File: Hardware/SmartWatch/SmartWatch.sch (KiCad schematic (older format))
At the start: 78 parts, among them IC1 6PAIC3109TWRHMRQ1, IC2 SPG08P4HM4H-1, IC3 MC3630, J1 Charging Port, J2 DA_PROG_CONN, J3 ARD_PROG_CONN, J4 Adafruit 4520, M1 c0720b001f, Q1 ECH8693R-TL-W, Q2 ECH8693R-TL-W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

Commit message: [Update] Changes to schematic and PCB test layout
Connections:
- net labels removed: LA
- wire segments 368 -> 371
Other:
- note added: "NOTE: After programming the chip, \nconnect the pads of JP1 with soldier.\n"
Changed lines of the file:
@@
 LX
 Text Label 4150 2950 0    50   ~ 0
-LA
+LY
 Wire Notes Line width 39 style solid rgb(0, 0, 0)
 	8850 500  8850 11200
@@
 L power:GND #PWR021
 U 1 1 6280EB46
-P 7000 10550
-F 0 "#PWR021" H 7000 10300 50  0001 C CNN
-F 1 "GND" H 7005 10377 50  0000 C CNN
-F 2 "" H 7000 10550 50  0001 C CNN
-F 3 "" H 7000 10550 50  0001 C CNN
-	1    7000 10550
+P 7000 10600
+F 0 "#PWR021" H 7000 10350 50  0001 C CNN
+F 1 "GND" H 7005 10427 50  0000 C CNN
+F 2 "" H 7000 10600 50  0001 C CNN
+F 3 "" H 7000 10600 50  0001 C CNN
+	1    7000 10600
 	1    0    0    -1
 $EndComp
@@
 L power:GND #PWR023
 U 1 1 6282AB30
-P 7650 10550
-F 0 "#PWR023" H 7650 10300 50  0001 C CNN
-F 1 "GND" H 7655 10377 50  0000 C CNN
-F 2 "" H 7650 10550 50  0001 C CNN
-F 3 "" H 7650 10550 50  0001 C CNN
-	1    7650 10550
+P 7650 10600
+F 0 "#PWR023" H 7650 10350 50  0001 C CNN
+F 1 "GND" H 7655 10427 50  0000 C CNN
+F 2 "" H 7650 10600 50  0001 C CNN
+F 3 "" H 7650 10600 50  0001 C CNN
+	1    7650 10600
 	1    0    0    -1
 $EndComp
@@
 L power:GND #PWR025
 U 1 1 628469D8
-P 8300 10550
-F 0 "#PWR025" H 8300 10300 50  0001 C CNN
-F 1 "GND" H 8305 10377 50  0000 C CNN
-F 2 "" H 8300 10550 50  0001 C CNN
-F 3 "" H 8300 10550 50  0001 C CNN
-	1    8300 10550
+P 8300 10600
+F 0 "#PWR025" H 8300 10350 50  0001 C CNN
+F 1 "GND" H 8305 10427 50  0000 C CNN
+F 2 "" H 8300 10600 50  0001 C CNN
+F 3 "" H 8300 10600 50  0001 C CNN
+	1    8300 10600
 	1    0    0    -1
 $EndComp
@@
 NoConn ~ 13750 3800
 $Comp
-L power:+3V3 #PWR?
+L power:+3V3 #PWR0121
 U 1 1 61E41A65
 P 9800 3250
-F 0 "#PWR?" H 9800 3100 50  0001 C CNN
+F 0 "#PWR0121" H 9800 3100 50  0001 C CNN
 F 1 "+3V3" V 9815 3378 50  0000 L CNN
 F 2 "" H 9800 3250 50  0001 C CNN
@@
 $EndComp
 $Comp
-L power:+3V3 #PWR?
+L power:+3V3 #PWR0146
 U 1 1 61E945E7
 P 9800 3750
-F 0 "#PWR?" H 9800 3600 50  0001 C CNN
+F 0 "#PWR0146" H 9800 3600 50  0001 C CNN
 F 1 "+3V3" V 9815 3878 50  0000 L CNN
 F 2 "" H 9800 3750 50  0001 C CNN
@@
 $EndComp
 $Comp
-L power:GND #PWR?
+L power:GND #PWR0147
 U 1 1 61EBD732
 P 9800 3650
-F 0 "#PWR?" H 9800 3400 50  0001 C CNN
+F 0 "#PWR0147" H 9800 3400 50  0001 C CNN
 F 1 "GND" V 9800 3450 50  0000 C CNN
 F 2 "" H 9800 3650 50  0001 C CNN
@@
 NoConn ~ 9800 2950
 $Comp
-L power:GNDREF #PWR?
+L power:GNDREF #PWR0148
 U 1 1 620BCE8F
 P 13150 4100
-F 0 "#PWR?" H 13150 3850 50  0001 C CNN
+F 0 "#PWR0148" H 13150 3850 50  0001 C CNN
 F 1 "GNDREF" H 13155 3927 50  0000 C CNN
 F 2 "" H 13150 4100 50  0001 C CNN
@@
 $EndComp
 $Comp
-L power:GNDREF #PWR?
+L power:GNDREF #PWR0149
 U 1 1 620E6DE9
 P 15300 3700
-F 0 "#PWR?" H 15300 3450 50  0001 C CNN
+F 0 "#PWR0149" H 15300 3450 50  0001 C CNN
 F 1 "GNDREF" H 15305 3527 50  0000 C CNN
 F 2 "" H 15300 3700 50  0001 C CNN
@@
 $EndComp
 $Comp
-L power:GNDREF #PWR?
+L power:GNDREF #PWR0150
 U 1 1 621114A5
 P 3750 5500
-F 0 "#PWR?" H 3750 5250 50  0001 C CNN
+F 0 "#PWR0150" H 3750 5250 50  0001 C CNN
 F 1 "GNDREF" H 3755 5327 50  0000 C CNN
 F 2 "" H 3750 5500 50  0001 C CNN
@@
 	1    0    0    -1
 $EndComp
+Text Notes 14350 1200 0    50   ~ 0
+NOTE: After programming the chip, \nconnect the pads of JP1 with soldier.\n
+Wire Wire Line
+	7000 10550 7000 10600
+Wire Wire Line
+	7650 10550 7650 10600
+Wire Wire Line
+	8300 10550 8300 10600
 $EndSCHEMATC

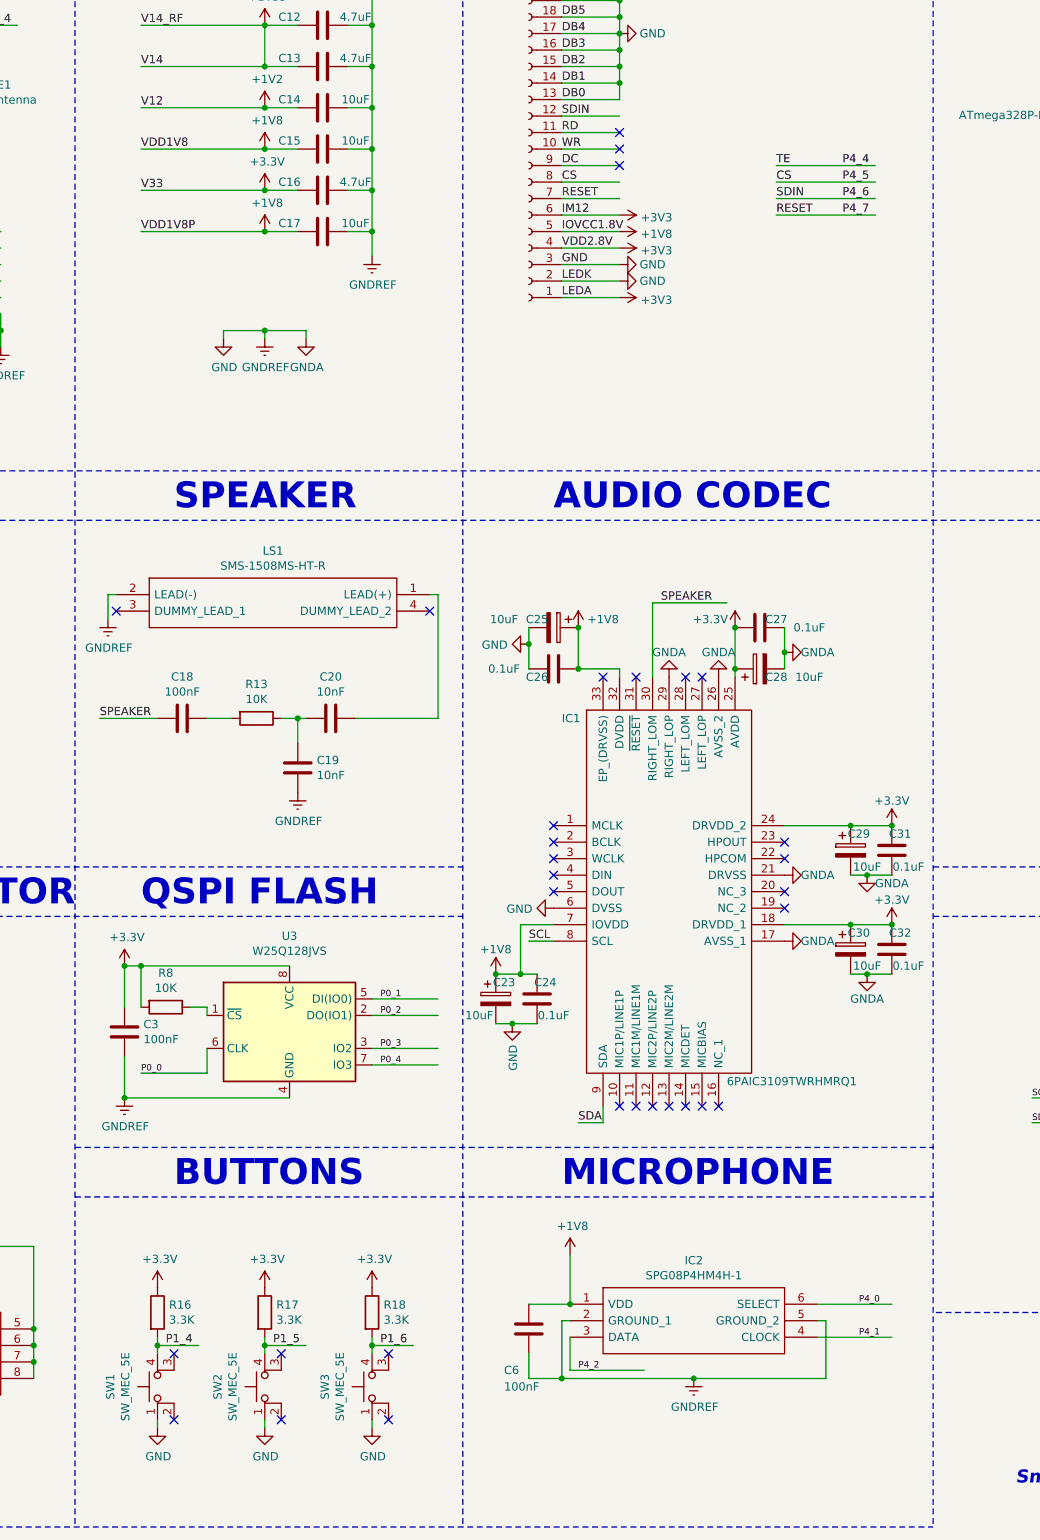
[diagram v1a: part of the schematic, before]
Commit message: [Update] Added communication with codec.
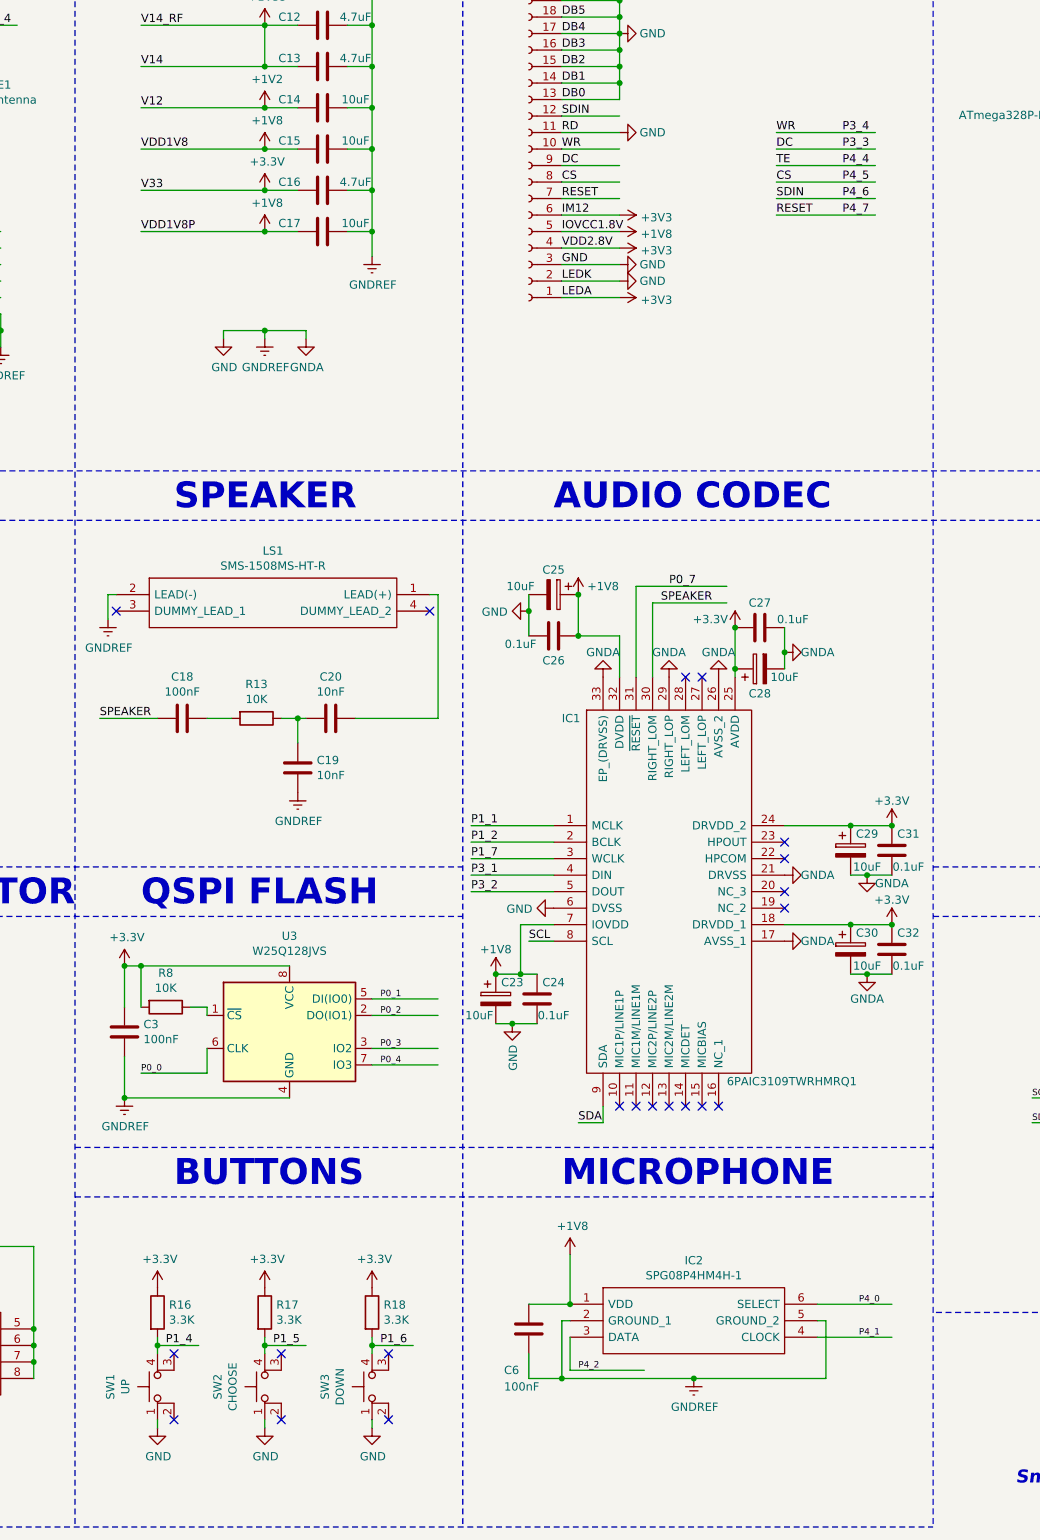
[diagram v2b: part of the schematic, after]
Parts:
- SW1: value SW_MEC_5E -> UP
- SW2: value SW_MEC_5E -> CHOOSE
- SW3: value SW_MEC_5E -> DOWN
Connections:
- wire segments 371 -> 380
- no-connect marks 58 -> 48
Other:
- moved on the sheet: C25, C26
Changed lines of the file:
@@
 U 1 1 630B89CE
 P 10650 5750
-F 0 "C27" V 10600 5850 50  0000 C CNN
-F 1 "0.1uF" V 10650 6050 50  0000 C CNN
+F 0 "C27" V 10500 5750 50  0000 C CNN
+F 1 "0.1uF" V 10600 5950 50  0000 C CNN
 F 2 "Capacitor_SMD:C_01005_0402Metric" H 10688 5600 50  0001 C CNN
 F 3 "~" H 10650 5750 50  0001 C CNN
@@
 U 1 1 6317A39A
 P 11450 7700
-F 0 "C32" H 11400 7600 50  0000 C CNN
+F 0 "C32" H 11350 7600 50  0000 C CNN
 F 1 "0.1uF" H 11350 7800 50  0000 C CNN
 F 2 "Capacitor_SMD:C_01005_0402Metric" H 11488 7550 50  0001 C CNN
@@
 U 1 1 630B9774
 P 10650 6000
-F 0 "C28" V 10600 5900 50  0000 C CNN
-F 1 "10uF" V 10600 5700 50  0000 C CNN
+F 0 "C28" V 10500 6000 50  0000 C CNN
+F 1 "10uF" V 10600 5850 50  0000 C CNN
 F 2 "Capacitor_SMD:C_01005_0402Metric" H 10688 5850 50  0001 C CNN
 F 3 "~" H 10650 6000 50  0001 C CNN
@@
 U 1 1 6317A3A0
 P 11200 7700
-F 0 "C30" H 11250 7800 50  0000 C CNN
+F 0 "C30" H 11300 7800 50  0000 C CNN
 F 1 "10uF" H 11300 7600 50  0000 C CNN
 F 2 "Capacitor_SMD:C_01005_0402Metric" H 11238 7550 50  0001 C CNN
@@
 U 1 1 632BFC59
 P 11450 7100
-F 0 "C31" H 11400 7000 50  0000 C CNN
+F 0 "C31" H 11350 7000 50  0000 C CNN
 F 1 "0.1uF" H 11350 7200 50  0000 C CNN
 F 2 "Capacitor_SMD:C_01005_0402Metric" H 11488 6950 50  0001 C CNN
@@
 U 1 1 632BFC60
 P 11200 7100
-F 0 "C29" H 11250 7200 50  0000 C CNN
+F 0 "C29" H 11300 7200 50  0000 C CNN
 F 1 "10uF" H 11300 7000 50  0000 C CNN
 F 2 "Capacitor_SMD:C_01005_0402Metric" H 11238 6950 50  0001 C CNN
@@
 L Device:C C26
 U 1 1 633C7CE9
-P 9400 6000
-F 0 "C26" V 9350 6100 50  0000 C CNN
-F 1 "0.1uF" V 9400 6300 50  0000 C CNN
-F 2 "Capacitor_SMD:C_01005_0402Metric" H 9438 5850 50  0001 C CNN
-F 3 "~" H 9400 6000 50  0001 C CNN
-	1    9400 6000
+P 9400 5800
+F 0 "C26" V 9250 5800 50  0000 C CNN
+F 1 "0.1uF" V 9350 6000 50  0000 C CNN
+F 2 "Capacitor_SMD:C_01005_0402Metric" H 9438 5650 50  0001 C CNN
+F 3 "~" H 9400 5800 50  0001 C CNN
+	1    9400 5800
 	0    -1   -1   0
 $EndComp
@@
 L Device:CP C25
 U 1 1 633C7CF8
-P 9400 5750
-F 0 "C25" V 9350 5650 50  0000 C CNN
-F 1 "10uF" V 9350 5450 50  0000 C CNN
-F 2 "Capacitor_SMD:C_01005_0402Metric" H 9438 5600 50  0001 C CNN
-F 3 "~" H 9400 5750 50  0001 C CNN
-	1    9400 5750
+P 9400 5550
+F 0 "C25" V 9250 5550 50  0000 C CNN
+F 1 "10uF" V 9350 5350 50  0000 C CNN
+F 2 "Capacitor_SMD:C_01005_0402Metric" H 9438 5400 50  0001 C CNN
+F 3 "~" H 9400 5550 50  0001 C CNN
+	1    9400 5550
 	0    1    1    0
 $EndComp
 Wire Wire Line
-	9550 6000 9550 5750
-Wire Wire Line
-	9250 6000 9250 5850
+	9550 5800 9550 5550
+Wire Wire Line
+	9250 5800 9250 5650
 $Comp
 L power:GND #PWR0133
 U 1 1 633EA102
-P 9250 5850
-F 0 "#PWR0133" H 9250 5600 50  0001 C CNN
-F 1 "GND" V 9255 5722 50  0000 R CNN
-F 2 "" H 9250 5850 50  0001 C CNN
-F 3 "" H 9250 5850 50  0001 C CNN
-	1    9250 5850
+P 9250 5650
+F 0 "#PWR0133" H 9250 5400 50  0001 C CNN
+F 1 "GND" V 9255 5522 50  0000 R CNN
+F 2 "" H 9250 5650 50  0001 C CNN
+F 3 "" H 9250 5650 50  0001 C CNN
+	1    9250 5650
 	0    1    1    0
 $EndComp
-Connection ~ 9250 5850
-Wire Wire Line
-	9250 5850 9250 5750
-Wire Wire Line
-	9800 6050 9800 6000
-Wire Wire Line
-	9800 6000 9550 6000
-Connection ~ 9550 6000
+Connection ~ 9250 5650
+Wire Wire Line
+	9250 5650 9250 5550
+Wire Wire Line
+	9800 5800 9550 5800
+Connection ~ 9550 5800
 $Comp
 L power:+1V8 #PWR0134
 U 1 1 6343113A
-P 9550 5750
-F 0 "#PWR0134" H 9550 5600 50  0001 C CNN
-F 1 "+1V8" H 9700 5800 50  0000 C CNN
-F 2 "" H 9550 5750 50  0001 C CNN
-F 3 "" H 9550 5750 50  0001 C CNN
-	1    9550 5750
-	1    0    0    -1
-$EndComp
-Connection ~ 9550 5750
+P 9550 5550
+F 0 "#PWR0134" H 9550 5400 50  0001 C CNN
+F 1 "+1V8" H 9700 5600 50  0000 C CNN
+F 2 "" H 9550 5550 50  0001 C CNN
+F 3 "" H 9550 5550 50  0001 C CNN
+	1    9550 5550
+	1    0    0    -1
+$EndComp
+Connection ~ 9550 5550
 $Comp
 L Device:C C24
 U 1 1 63433612
 P 9300 8000
-F 0 "C24" H 9250 7900 50  0000 C CNN
+F 0 "C24" H 9200 7900 50  0000 C CNN
 F 1 "0.1uF" H 9200 8100 50  0000 C CNN
 F 2 "Capacitor_SMD:C_01005_0402Metric" H 9338 7850 50  0001 C CNN
@@
 U 1 1 63433618
 P 9050 8000
-F 0 "C23" H 9100 8100 50  0000 C CNN
+F 0 "C23" H 9150 8100 50  0000 C CNN
 F 1 "10uF" H 8950 7900 50  0000 C CNN
 F 2 "Capacitor_SMD:C_01005_0402Metric" H 9088 7850 50  0001 C CNN
@@
 P 7100 10350
 F 0 "SW1" H 7100 10735 50  0000 C CNN
-F 1 "SW_MEC_5E" H 7100 10644 50  0000 C CNN
+F 1 "UP" H 7100 10644 50  0000 C CNN
 F 2 "Button_Switch_THT:SW_Tactile_SPST_Angled_PTS645Vx58-2LFS" H 7100 10650 50  0001 C CNN
 F 3 "http://www.apem.com/int/index.php?controller=attachment&id_attachment=1371" H 7100 10650 50  0001 C CNN
@@
 P 7750 10350
 F 0 "SW2" H 7750 10735 50  0000 C CNN
-F 1 "SW_MEC_5E" H 7750 10644 50  0000 C CNN
+F 1 "CHOOSE" H 7750 10644 50  0000 C CNN
 F 2 "Button_Switch_THT:SW_Tactile_SPST_Angled_PTS645Vx58-2LFS" H 7750 10650 50  0001 C CNN
 F 3 "http://www.apem.com/int/index.php?controller=attachment&id_attachment=1371" H 7750 10650 50  0001 C CNN
@@
 P 8400 10350
 F 0 "SW3" H 8400 10735 50  0000 C CNN
-F 1 "SW_MEC_5E" H 8400 10644 50  0000 C CNN
+F 1 "DOWN" H 8400 10644 50  0000 C CNN
 F 2 "Button_Switch_THT:SW_Tactile_SPST_Angled_PTS645Vx58-2LFS" H 8400 10650 50  0001 C CNN
 F 3 "http://www.apem.com/int/index.php?controller=attachment&id_attachment=1371" H 8400 10650 50  0001 C CNN
@@
 NoConn ~ 10300 8650
 NoConn ~ 10400 8650
-NoConn ~ 9400 7350
-NoConn ~ 9400 7250
-NoConn ~ 9400 6950
-NoConn ~ 9400 7050
-NoConn ~ 9400 7150
 NoConn ~ 10800 7050
 NoConn ~ 10800 7150
@@
 NoConn ~ 10300 6050
 NoConn ~ 10200 6050
-NoConn ~ 9900 6050
-NoConn ~ 9700 6050
 NoConn ~ 8650 5650
 NoConn ~ 6750 5650
@@
 Text Label 11150 2950 0    50   ~ 0
 P4_4
-NoConn ~ 9800 2850
-NoConn ~ 9800 2750
-NoConn ~ 9800 2950
 $Comp
 L power:GNDREF #PWR0148
@@
 Wire Wire Line
 	8300 10550 8300 10600
+Wire Wire Line
+	10750 2850 11350 2850
+Text Label 10750 2850 0    50   ~ 0
+DC
+Text Label 11150 2850 0    50   ~ 0
+P3_3
+Wire Wire Line
+	10750 2750 11350 2750
+Text Label 10750 2750 0    50   ~ 0
+WR
+Text Label 11150 2750 0    50   ~ 0
+P3_4
+$Comp
+L power:GND #PWR?
+U 1 1 61ECD16D
+P 9800 2750
+F 0 "#PWR?" H 9800 2500 50  0001 C CNN
+F 1 "GND" V 9800 2550 50  0000 C CNN
+F 2 "" H 9800 2750 50  0001 C CNN
+F 3 "" H 9800 2750 50  0001 C CNN
+	1    9800 2750
+	0    -1   -1   0
+$EndComp
+Wire Wire Line
+	9800 5800 9800 6050
+$Comp
+L power:GNDA #PWR?
+U 1 1 61F336D3
+P 9700 6050
+F 0 "#PWR?" H 9700 5800 50  0001 C CNN
+F 1 "GNDA" H 9700 5900 50  0000 C CNN
+F 2 "" H 9700 6050 50  0001 C CNN
+F 3 "" H 9700 6050 50  0001 C CNN
+	1    9700 6050
+	-1   0    0    1
+$EndComp
+Wire Wire Line
+	9900 6050 9900 5500
+Wire Wire Line
+	9900 5500 10450 5500
+Text Label 10100 5500 0    50   ~ 0
+P0_7
+Wire Wire Line
+	9400 6950 8900 6950
+Wire Wire Line
+	9400 7050 8900 7050
+Wire Wire Line
+	9400 7150 8900 7150
+Wire Wire Line
+	9400 7250 8900 7250
+Wire Wire Line
+	9400 7350 8900 7350
+Text Label 8900 6950 0    50   ~ 0
+P1_1
+Text Label 8900 7050 0    50   ~ 0
+P1_2
+Text Label 8900 7150 0    50   ~ 0
+P1_7
+Text Label 8900 7250 0    50   ~ 0
+P3_1
+Text Label 8900 7350 0    50   ~ 0
+P3_2
 $EndSCHEMATC

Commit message: [Update] Schematic for review.
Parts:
- removed SW1: UP, Button_Switch_THT:SW_Tactile_SPST_Angled_PTS645Vx58-2LFS, symbol Switch:SW_MEC_5E
- removed SW2: CHOOSE, Button_Switch_THT:SW_Tactile_SPST_Angled_PTS645Vx58-2LFS, symbol Switch:SW_MEC_5E
- removed SW3: DOWN, Button_Switch_THT:SW_Tactile_SPST_Angled_PTS645Vx58-2LFS, symbol Switch:SW_MEC_5E
- added SW1: UP, Button_Switch_THT:SW_Tactile_SPST_Angled_PTS645Vx58-2LFS, symbol Switch:SW_MEC_5G
- added SW2: CHOOSE, Button_Switch_THT:SW_Tactile_SPST_Angled_PTS645Vx58-2LFS, symbol Switch:SW_MEC_5G
- added SW3: DOWN, Button_Switch_THT:SW_Tactile_SPST_Angled_PTS645Vx58-2LFS, symbol Switch:SW_MEC_5G
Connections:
- no-connect marks 48 -> 42
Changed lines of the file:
@@
 Wire Wire Line
 	5900 2650 5850 2650
-Text Label 5350 2650 0    50   ~ 0
-RFIOP
-Wire Wire Line
-	5550 2650 5350 2650
 $Comp
 L Device:C C22
@@
 Connection ~ 5900 2650
 $Comp
-L Device:C C21
-U 1 1 61DC6589
-P 5550 2800
-F 0 "C21" H 5550 2900 50  0000 L CNN
-F 1 "C" H 5550 2700 50  0000 L CNN
-F 2 "Capacitor_SMD:C_01005_0402Metric" H 5588 2650 50  0001 C CNN
-F 3 "~" H 5550 2800 50  0001 C CNN
-	1    5550 2800
-	1    0    0    -1
-$EndComp
-$Comp
-L power:GNDREF #PWR0123
-U 1 1 61DDB960
-P 5550 2950
-F 0 "#PWR0123" H 5550 2700 50  0001 C CNN
-F 1 "GNDREF" H 5555 2777 50  0000 C CNN
-F 2 "" H 5550 2950 50  0001 C CNN
-F 3 "" H 5550 2950 50  0001 C CNN
-	1    5550 2950
-	1    0    0    -1
-$EndComp
-$Comp
 L power:GNDREF #PWR0124
 U 1 1 61E059F0
@@
 	1    0    0    -1
 $EndComp
-Connection ~ 5550 2650
 Wire Notes Line width 39 style solid rgb(0, 0, 0)
 	500  800  16000 800
@@
 	0    1    1    0
 $EndComp
-$Comp
-L Switch:SW_MEC_5E SW1
-U 1 1 61E3665D
-P 7100 10350
-F 0 "SW1" H 7100 10735 50  0000 C CNN
-F 1 "UP" H 7100 10644 50  0000 C CNN
-F 2 "Button_Switch_THT:SW_Tactile_SPST_Angled_PTS645Vx58-2LFS" H 7100 10650 50  0001 C CNN
-F 3 "http://www.apem.com/int/index.php?controller=attachment&id_attachment=1371" H 7100 10650 50  0001 C CNN
-	1    7100 10350
-	0    -1   -1   0
-$EndComp
-$Comp
-L Switch:SW_MEC_5E SW2
-U 1 1 61E380F9
-P 7750 10350
-F 0 "SW2" H 7750 10735 50  0000 C CNN
-F 1 "CHOOSE" H 7750 10644 50  0000 C CNN
-F 2 "Button_Switch_THT:SW_Tactile_SPST_Angled_PTS645Vx58-2LFS" H 7750 10650 50  0001 C CNN
-F 3 "http://www.apem.com/int/index.php?controller=attachment&id_attachment=1371" H 7750 10650 50  0001 C CNN
-	1    7750 10350
-	0    -1   -1   0
-$EndComp
-$Comp
-L Switch:SW_MEC_5E SW3
-U 1 1 61E6124E
-P 8400 10350
-F 0 "SW3" H 8400 10735 50  0000 C CNN
-F 1 "DOWN" H 8400 10644 50  0000 C CNN
-F 2 "Button_Switch_THT:SW_Tactile_SPST_Angled_PTS645Vx58-2LFS" H 8400 10650 50  0001 C CNN
-F 3 "http://www.apem.com/int/index.php?controller=attachment&id_attachment=1371" H 8400 10650 50  0001 C CNN
-	1    8400 10350
-	0    -1   -1   0
-$EndComp
-NoConn ~ 7100 10550
-NoConn ~ 7100 10150
-NoConn ~ 7750 10150
-NoConn ~ 7750 10550
-NoConn ~ 8400 10550
-NoConn ~ 8400 10150
 NoConn ~ 9800 8650
 NoConn ~ 9900 8650
@@
 P3_4
 $Comp
-L power:GND #PWR?
+L power:GND #PWR028
 U 1 1 61ECD16D
 P 9800 2750
-F 0 "#PWR?" H 9800 2500 50  0001 C CNN
+F 0 "#PWR028" H 9800 2500 50  0001 C CNN
 F 1 "GND" V 9800 2550 50  0000 C CNN
 F 2 "" H 9800 2750 50  0001 C CNN
@@
 	9800 5800 9800 6050
 $Comp
-L power:GNDA #PWR?
+L power:GNDA #PWR027
 U 1 1 61F336D3
 P 9700 6050
-F 0 "#PWR?" H 9700 5800 50  0001 C CNN
+F 0 "#PWR027" H 9700 5800 50  0001 C CNN
 F 1 "GNDA" H 9700 5900 50  0000 C CNN
 F 2 "" H 9700 6050 50  0001 C CNN
@@
 Text Label 8900 7350 0    50   ~ 0
 P3_2
+$Comp
+L Switch:SW_MEC_5G SW1
+U 1 1 61EEDF3D
+P 7000 10350
+F 0 "SW1" V 7046 10302 50  0000 R CNN
+F 1 "UP" V 6955 10302 50  0000 R CNN
+F 2 "Button_Switch_THT:SW_Tactile_SPST_Angled_PTS645Vx58-2LFS" H 7000 10550 50  0001 C CNN
+F 3 "http://www.apem.com/int/index.php?controller=attachment&id_attachment=488" H 7000 10550 50  0001 C CNN
+	1    7000 10350
+	0    -1   -1   0
+$EndComp
+$Comp
+L Switch:SW_MEC_5G SW2
+U 1 1 61F47DF6
+P 7650 10350
+F 0 "SW2" V 7696 10302 50  0000 R CNN
+F 1 "CHOOSE" V 7605 10302 50  0000 R CNN
+F 2 "Button_Switch_THT:SW_Tactile_SPST_Angled_PTS645Vx58-2LFS" H 7650 10550 50  0001 C CNN
+F 3 "http://www.apem.com/int/index.php?controller=attachment&id_attachment=488" H 7650 10550 50  0001 C CNN
+	1    7650 10350
+	0    -1   -1   0
+$EndComp
+$Comp
+L Switch:SW_MEC_5G SW3
+U 1 1 61F74894
+P 8300 10350
+F 0 "SW3" V 8346 10302 50  0000 R CNN
+F 1 "DOWN" V 8255 10302 50  0000 R CNN
+F 2 "Button_Switch_THT:SW_Tactile_SPST_Angled_PTS645Vx58-2LFS" H 8300 10550 50  0001 C CNN
+F 3 "http://www.apem.com/int/index.php?controller=attachment&id_attachment=488" H 8300 10550 50  0001 C CNN
+	1    8300 10350
+	0    -1   -1   0
+$EndComp
+$Comp
+L power:GNDREF #PWR0123
+U 1 1 61DDB960
+P 5550 2950
+F 0 "#PWR0123" H 5550 2700 50  0001 C CNN
+F 1 "GNDREF" H 5555 2777 50  0000 C CNN
+F 2 "" H 5550 2950 50  0001 C CNN
+F 3 "" H 5550 2950 50  0001 C CNN
+	1    5550 2950
+	1    0    0    -1
+$EndComp
+$Comp
+L Device:C C21
+U 1 1 61DC6589
+P 5550 2800
+F 0 "C21" H 5550 2900 50  0000 L CNN
+F 1 "C" H 5550 2700 50  0000 L CNN
+F 2 "Capacitor_SMD:C_01005_0402Metric" H 5588 2650 50  0001 C CNN
+F 3 "~" H 5550 2800 50  0001 C CNN
+	1    5550 2800
+	1    0    0    -1
+$EndComp
+Connection ~ 5550 2650
+Wire Wire Line
+	5550 2650 5350 2650
+Text Label 5350 2650 0    50   ~ 0
+RFIOP
 $EndSCHEMATC
